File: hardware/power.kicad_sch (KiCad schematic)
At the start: 31 parts, among them J2 batt, Q1 NPN SS8050, SW57 MK-12C02-G020, U3 BQ24075RGT, U4 TLV62569DBV

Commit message: use AO3400A in place of the npn
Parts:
- removed Q1: NPN SS8050, Package_TO_SOT_SMD:SOT-23, symbol Device:Q_NPN_BEC
- added Q1: AO3400A, Package_TO_SOT_SMD:SOT-23, symbol Transistor_FET:AO3400A
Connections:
- net CHG: now also Q1.3 (D)
- net GND: now also Q1.2 (S)
- net ~{CHG}: now also Q1.1 (G)
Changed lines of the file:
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@@
-	)
-	(symbol
-		(lib_id "Device:Q_NPN_BEC")
-		(at 237.49 95.25 0)
-		(unit 1)
-		(exclude_from_sim no)
-		(in_bom yes)
-		(on_board yes)
-		(dnp no)
-		(fields_autoplaced yes)
-		(property "Reference" "Q1"
-			(at 242.57 93.9799 0)
-			(effects
-				(font
-					(size 1.27 1.27)
-				)
-				(justify left)
-			)
-		)
-		(property "Value" "NPN SS8050"
-			(at 242.57 96.5199 0)
-			(effects
-				(font
-					(size 1.27 1.27)
-				)
-				(justify left)
-			)
-		)
-		(property "Footprint" "Package_TO_SOT_SMD:SOT-23"
-			(at 242.57 92.71 0)
-			(effects
-				(font
-					(size 1.27 1.27)
-				)
-				(hide yes)
-			)
-		)
-		(property "Datasheet" "~"
-			(at 237.49 95.25 0)
-			(effects
-				(font
-					(size 1.27 1.27)
-				)
-				(hide yes)
-			)
-		)
-		(property "Description" "NPN transistor, base/emitter/collector"
-			(at 237.49 95.25 0)
-			(effects
-				(font
-					(size 1.27 1.27)
-				)
-				(hide yes)
-			)
-		)
-		(property "LCSC" "C2150"
-			(at 237.49 95.25 0)
-			(effects
-				(font
-					(size 1.27 1.27)
-				)
-				(hide yes)
-			)
-		)
-		(pin "1"
-		)
-		(pin "3"
-		)
-		(pin "2"
-		)
-		(instances
-			(project "badge"
-				(path "/dc4a3d77-b0f8-4e90-a4be-3e93c7025348/fa1edb42-107e-4301-94d6-2222638475c5"
-					(reference "Q1")
-					(unit 1)
-				)
-			)
-		)
 	)
 	(symbol
@@
 					(unit 1)
 				)
+			)
+		)
+	)
+	(symbol
+		(lib_id "Transistor_FET:AO3400A")
+		(at 237.49 95.25 0)
+		(unit 1)
+		(exclude_from_sim no)
+		(in_bom yes)
+		(on_board yes)
+		(dnp no)
+		(fields_autoplaced yes)
+		(property "Reference" "Q1"
+			(at 243.84 93.9799 0)
+			(effects
+				(font
+					(size 1.27 1.27)
+				)
+				(justify left)
+			)
+		)
+		(property "Value" "AO3400A"
+			(at 243.84 96.5199 0)
+			(effects
+				(font
+					(size 1.27 1.27)
+				)
+				(justify left)
+			)
+		)
+		(property "Footprint" "Package_TO_SOT_SMD:SOT-23"
+			(at 242.57 97.155 0)
+			(effects
+				(font
+					(size 1.27 1.27)
+					(italic yes)
+				)
+				(justify left)
+				(hide yes)
+			)
+		)
+		(property "Datasheet" "http://www.aosmd.com/pdfs/datasheet/AO3400A.pdf"
+			(at 242.57 99.06 0)
+			(effects
+				(font
+					(size 1.27 1.27)
+				)
+				(justify left)
+				(hide yes)
+			)
+		)
+		(property "Description" "30V Vds, 5.7A Id, N-Channel MOSFET, SOT-23"
+			(at 237.49 95.25 0)
+			(effects
+				(font
+					(size 1.27 1.27)
+				)
+				(hide yes)
+			)
+		)
+		(property "LCSC" "C20917"
+			(at 237.49 95.25 0)
+			(effects
+				(font
+					(size 1.27 1.27)
+				)
+				(hide yes)
+			)
+		)
+		(pin "1"
+		)
+		(pin "2"
+		)
+		(pin "3"
+		)
+		(instances
+			(project "badge"
+				(path "/dc4a3d77-b0f8-4e90-a4be-3e93c7025348/fa1edb42-107e-4301-94d6-2222638475c5"
+					(reference "Q1")
+					(unit 1)
+				)

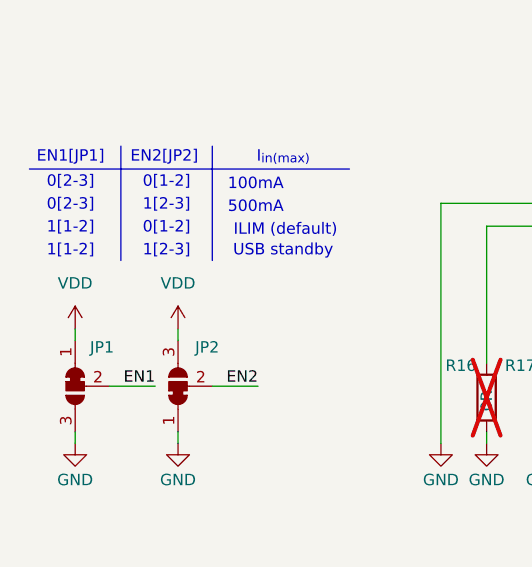
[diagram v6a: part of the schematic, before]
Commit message: Routhe BMS subsystem
Fix the JP1 and JP2 power net
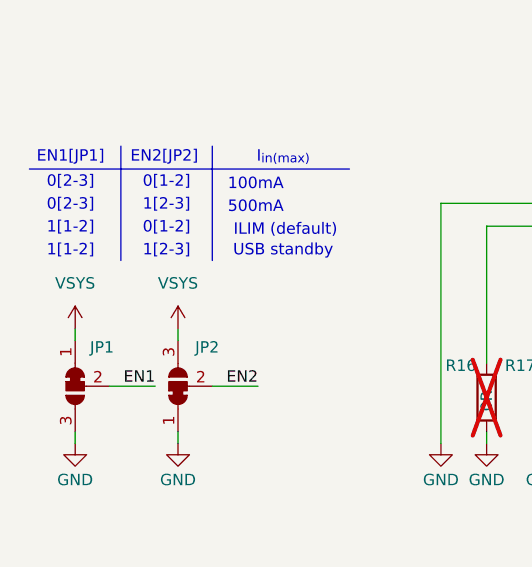
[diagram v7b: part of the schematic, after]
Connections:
- net VDD is gone; now on net VSYS: JP1.1 (A), JP2.3 (B)

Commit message: Route the audio subsystem
Fix BMS routing
Remove audio gain selection, to relax routing
Add DRC rule for JLC
Add custom rule for Audio BGA routing
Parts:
- U3: footprint Package_DFN_QFN:VQFN-16-1EP_3x3mm_P0.5mm_EP1.6x1.6mm -> Package_DFN_QFN:VQFN-16-1EP_3x3mm_P0.5mm_EP1.6x1.6mm_ThermalVias
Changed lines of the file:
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@@
 			)
 		)
-		(property "Footprint" "Package_DFN_QFN:VQFN-16-1EP_3x3mm_P0.5mm_EP1.6x1.6mm"
+		(property "Footprint" "Package_DFN_QFN:VQFN-16-1EP_3x3mm_P0.5mm_EP1.6x1.6mm_ThermalVias"
 			(at 110.49 151.13 0)
 			(effects
